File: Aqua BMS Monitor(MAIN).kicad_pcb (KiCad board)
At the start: 4 copper layers, 142 x 101.5 mm, 242 parts, among them J1 UART Jpins, J2 XT60PW-M, J3 XT60PW-M, J4 XT60PW-M, J5 SWD_01x04_Pin, J6 XT60PW-M, J7 USB_C_Female_USB2_Small, Q6 NPN, U1 BQ7695202, U2 STM32F205RETx, U4 LM66100DCKR, U5 LM66100DCKR, U6 LM66100DCKR, U7 LTC4359-DCB, U9 AMS1117-3.3, X1 X322516MRB4SI

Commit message: Not sure
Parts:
- moved U5 30.2 mm to (199.5, 81.7), turned to 0 degrees
- moved C71 30.1 mm to (199.3, 83.8), turned to 0 degrees
- moved U9 18.3 mm to (193.5, 82.2), turned to 0 degrees
- moved TP23 14.0 mm to (222.0, 90.5)
- moved TP5 14.0 mm to (222.0, 95.0)
- moved TP64 14.0 mm to (221.5, 84.0)
- moved TP65 14.0 mm to (221.5, 87.0)
- moved USBC1 9.84 mm to (188.0, 84.7), turned to -90 degrees
- moved USBC2 7.54 mm to (188.0, 80.2), turned to 90 degrees
- moved TP62 7.23 mm to (182.8, 82.7)
- moved USBR3 5.11 mm to (182.8, 90.5)
- moved MCUC14 4.73 mm to (180.8, 89.3), turned to 0 degrees
- moved MCUC21 4.46 mm to (179.2, 87.7)
- moved C72 3.41 mm to (158.1, 87.5)
- moved FB1 3.41 mm to (164.4, 83.0)
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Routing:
- net BAT-: track 221.2 -> 200.9 mm, vias 91 -> 90
- net REG1: track 10.7 -> 23.0 mm, vias 0 -> 2
- net USB_C_VBUS: track 30.0 -> 20.8 mm
- net VDD: track 170.7 -> 176.9 mm
- net ALERT: track 9.13 -> 4.34 mm, vias 1 -> 0
- net Net-(U2-BOOT0): track 47.4 -> 49.0 mm
- net Net-(U2-NRST): track 37.0 -> 36.1 mm

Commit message: Aight
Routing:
- net BAT-: track 200.9 -> 204.9 mm, vias 90 -> 93
- net VDD: track 176.9 -> 178.5 mm
- added copper zone on In2.Cu, net BAT-

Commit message: Final for now
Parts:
- added MCUTVS3: PTVSUC3D5VB, easyeda2kicad:5V_TVS_SOD-323_L1.8-W1.3-LS2.5-BI, F.Cu at (201.8, 100.5)
- added MCUTVS4: PTVSUC3D5VB, easyeda2kicad:5V_TVS_SOD-323_L1.8-W1.3-LS2.5-BI, F.Cu at (204.5, 97.5)
- added TP3: CONN-TP, TestPoint:TestPoint_Pad_1.5x1.5mm, F.Cu at (145.0, 90.5)
- moved TP25 46.6 mm to (164.5, 81.3)
- moved TP24 45.5 mm to (164.4, 86.4)
- moved TP65 43.6 mm to (185.2, 111.1)
- moved TP63 42.8 mm to (154.1, 91.0)
- moved TP70 36.4 mm to (163.9, 100.6)
- moved TP68 35.8 mm to (160.7, 98.8)
- moved TP61 34.4 mm to (177.6, 105.1)
- moved TP64 33.7 mm to (202.5, 111.8)
- moved TP72 32.5 mm to (155.9, 93.5)
- moved TP71 30.0 mm to (158.2, 97.5)
- moved TP5 22.9 mm to (199.7, 99.9)
- moved TP69 22.5 mm to (156.6, 105.1)
- moved TP66 21.5 mm to (156.8, 111.3)
- moved TP23 20.6 mm to (202.2, 96.3)
- moved TP67 14.7 mm to (170.2, 111.3)
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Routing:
- net CFETOFF: track 0.00 -> 51.9 mm, vias 0 -> 2
- net ALERT: track 4.34 -> 51.4 mm, vias 0 -> 4
- net DCHG: track 4.77 -> 48.4 mm, vias 1 -> 3
- net DDSG: track 2.49 -> 40.2 mm, vias 0 -> 3
- net RST_SHUT: track 3.80 -> 37.2 mm, vias 1 -> 3
- net DFETOFF: track 1.71 -> 34.6 mm, vias 1 -> 2
- net MCUCFETOFF: track 0.00 -> 28.4 mm, vias 0 -> 3
- net MCUDFETOFF: track 8.14 -> 22.7 mm, vias 1 -> 2
- net Net-(DD1-K): track 32.5 -> 41.7 mm
- net USART1_RX: track 25.7 -> 34.6 mm
- net VDD: track 178.5 -> 171.7 mm
- net Net-(U2-BOOT0): track 49.0 -> 53.9 mm
- net Net-(U2-VCAP_1): track 1.82 -> 6.32 mm
- net Net-(U2-NRST): track 36.1 -> 39.4 mm
- net SCL: track 24.7 -> 26.7 mm
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- added copper zone on In1.Cu, net BAT-
- removed copper zone on In2.Cu, net BAT-
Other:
- board text added: "U1"

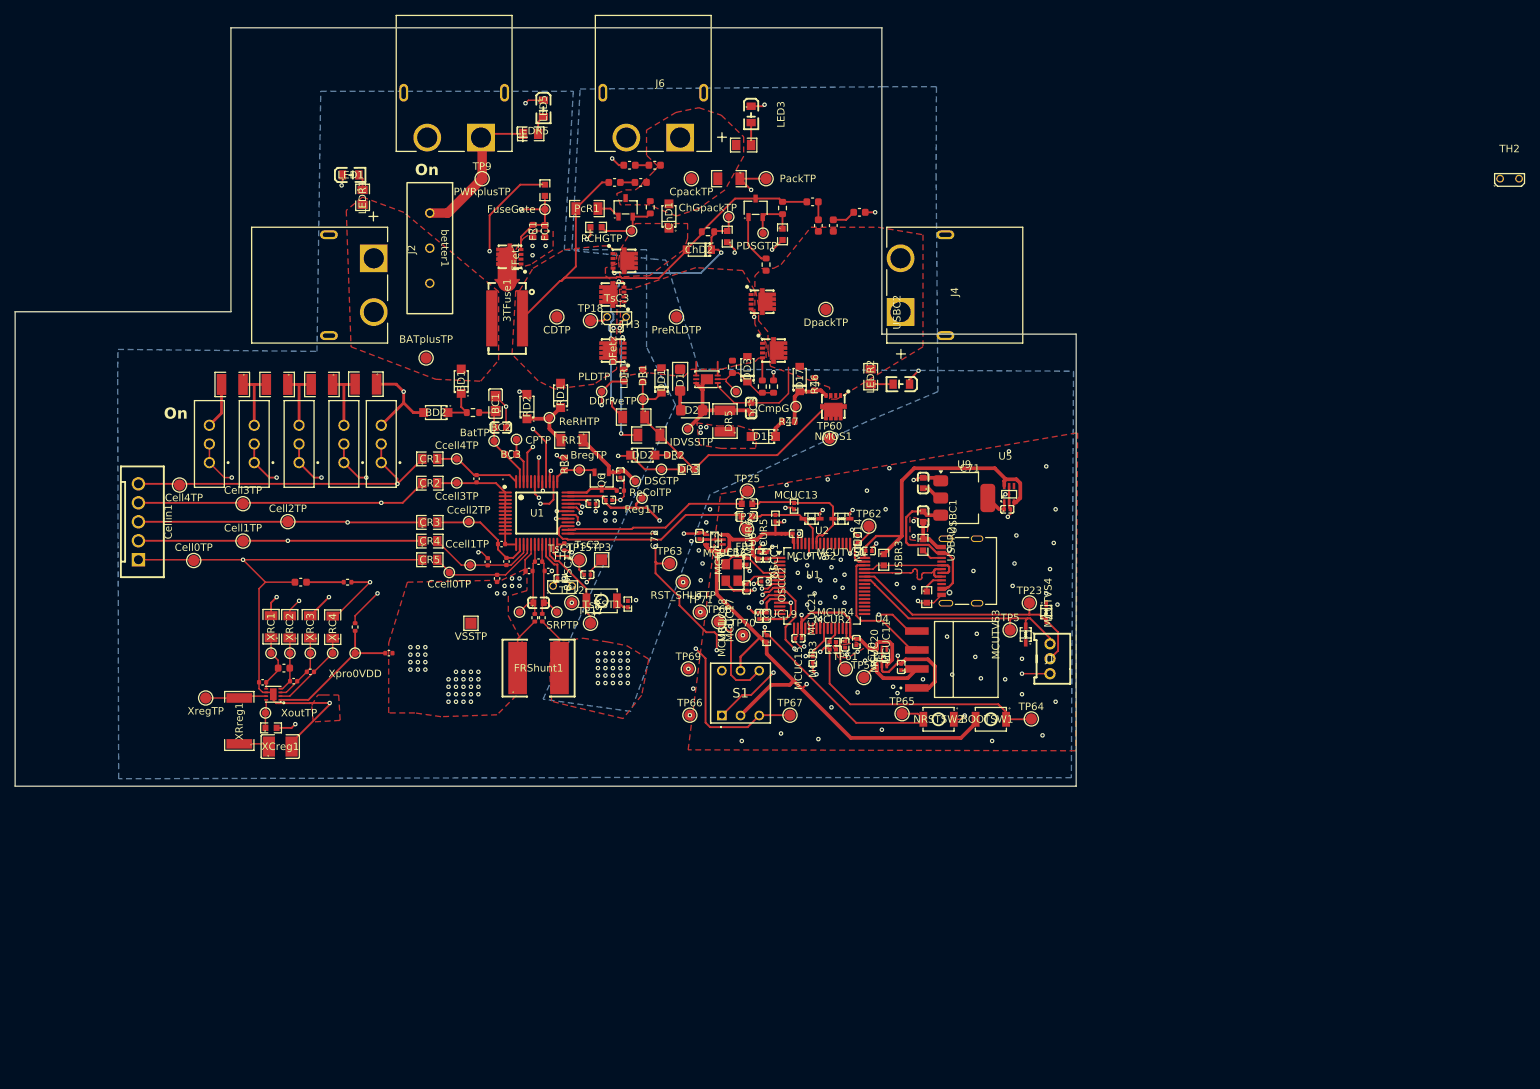
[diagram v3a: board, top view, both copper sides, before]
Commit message: Couple fixes
- Fixed ground plane
- changed thermistor placement
- Attached floating components
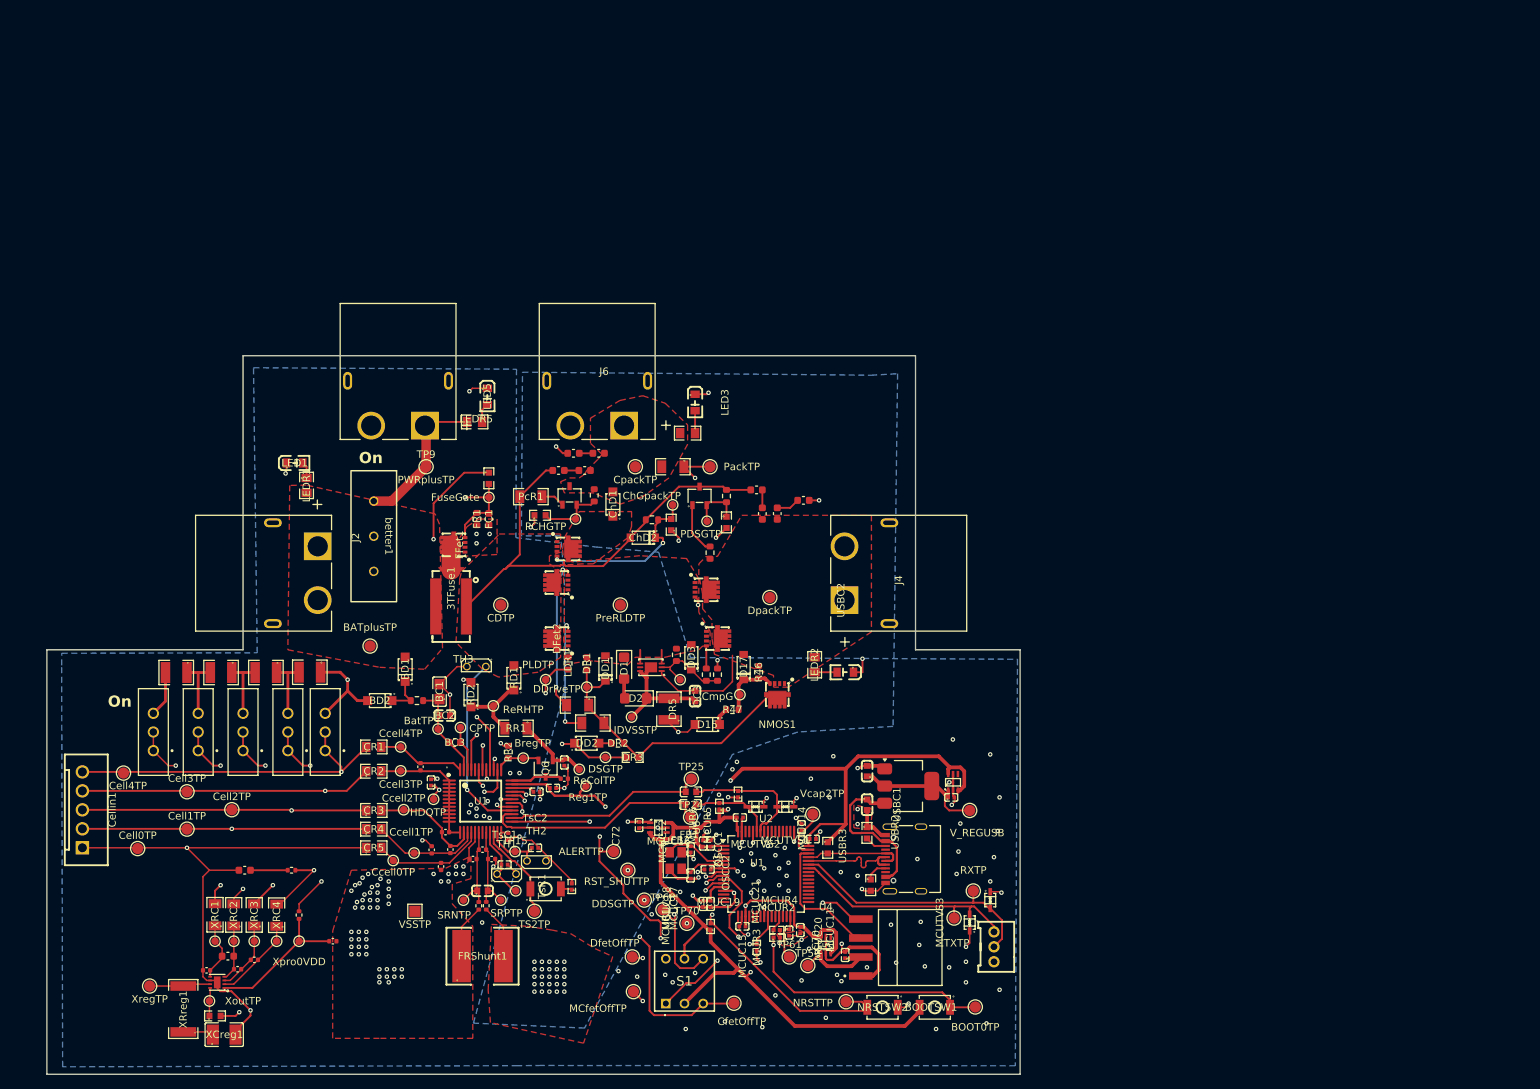
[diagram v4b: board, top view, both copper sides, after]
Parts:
- removed TP3: CONN-TP, TestPoint:TestPoint_Pad_1.5x1.5mm
- TP12, TP15, TP18: footprint TestPoint:TestPoint_Pad_D1.5mm -> TestPoint:TestPoint_Pad_D1.0mm
- moved TH2 159.0 mm to (136.3, 130.8)
- moved TP18 67.4 mm to (122.5, 122.5)
- moved TsC3 65.7 mm to (122.2, 120.3), turned to 90 degrees
- moved TP60 53.2 mm to (194.2, 124.0)
- moved TH3 50.4 mm to (128.2, 104.8), turned to 180 degrees
- moved TP15 40.0 mm to (133.4, 129.6)
- moved C72 39.5 mm to (150.0, 126.0)
- moved TP34 39.5 mm to (118.5, 124.0)
- moved BMSC1 39.5 mm to (132.5, 127.5)
- moved MCUC19 39.3 mm to (159.2, 131.9)
- moved SC2 39.3 mm to (130.3, 130.6)
- moved BC1 39.3 mm to (123.3, 108.2)
- moved BD1 39.3 mm to (118.7, 105.2)
- moved BQ296115DSGR1 39.3 mm to (93.5, 147.1)
- moved C1-0 39.3 mm to (123.5, 131.6)
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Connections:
- U1 pad 44: SCL -> unconnected-(U1-NC-Pad44)
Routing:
- net VDD: track 171.7 -> 191.4 mm, vias 6 -> 7
- net BAT-: track 206.4 -> 222.8 mm, vias 156 -> 170
- net HDQ: track 19.1 -> 31.3 mm, vias 1 -> 2
- net V_REGUSB: track 6.60 -> 18.1 mm
- net Net-(U2-BOOT0): track 53.9 -> 51.3 mm
- net Net-(U2-NRST): track 39.4 -> 41.8 mm
- net SWCLK: track 17.1 -> 18.7 mm
- net Net-(RD1-K): track 8.68 -> 10.2 mm
- net Net-(U1-FUSE): track 55.9 -> 55.2 mm
- net PACK-: track 14.6 -> 15.3 mm
- net MCUCFETOFF: track 28.4 -> 29.1 mm
- net Net-(Dfet1-G): track 21.0 -> 20.4 mm
- net TS3: track 7.25 -> 7.87 mm
- net TS1: track 10.1 -> 9.86 mm, vias 1 -> 0
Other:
- board size 142 x 101.5 mm -> 130.2 x 96.2 mm
- board text added: "Should we have an R here to deter the current path"
- board text removed: "Charge and discharge"
- board text removed: "Clamp"
- board text removed: "MCU"
- board text removed: "Pre-Discharge Charge"
- board text removed: "Shunt resistor setup"
- board text removed: "TPs"
- board text removed: "Thermal measurement"

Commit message: Decorating
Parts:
- added G***: LOGO, easyeda2kicad:Eagle Battery, B.Cu at (138.0, 90.0)
- added G***: LOGO, easyeda2kicad:Aqua Logo, B.Cu at (133.0, 120.8)
- TP37: value Xpro0VDD -> Xpro0VDDTP
- TP51: value PLDTP -> LDTP
- TP53: value CmpG -> CmpGTP
- TP60: value V_REGUSB -> V_REGUSBTP
- TP62: value Vcap2TP -> VCAP2TP
- moved TP66 1.53 mm to (148.8, 149.8)
- renumbered BOOTSW1 to BOOT0, TP70 to DCHGTP, TP68 to MCUDFETOFFTP, NRSTSW2 to RESET, TP25 to SCLTP, TP24 to SDATP, TP12 to TS1TP, TP15 to TS3TP, TP61 to VCAP1TP, TP59 to V_SWDTP
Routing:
- net BAT-: vias 170 -> 171
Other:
- board text added: "Battery Management System (BMS) Board aQuatonomous August 2026 Logan Calder Alisa Ruzhynsky"

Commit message: coupla changes
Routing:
- net BAT-: track 222.8 -> 316.4 mm
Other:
- board text removed: "Should we have an R here to deter the current path"
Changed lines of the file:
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@@
 		(property "Reference" "TP57"
 			(at 0 -1.448 0)
-			(layer "F.SilkS")
+			(layer "F.Fab")
 			(hide yes)
 			(effects
@@
 		)
 		(property "Value" "IDGTP"
-			(at 0 1.55 0)
-			(layer "F.Fab")
-			(hide yes)
+			(at -2.9 0.45 0)
+			(layer "F.SilkS")
 			(effects
 				(font
@@
 		(property "Reference" "TP40"
 			(at 0 -1.448 0)
-			(layer "F.SilkS")
+			(layer "F.Fab")
 			(hide yes)
 			(effects
@@
 		)
 		(property "Value" "Xcel1TP"
-			(at 0 1.55 0)
-			(layer "F.Fab")
-			(hide yes)
+			(at -5.45 -0.15 0)
+			(layer "F.SilkS")
 			(effects
 				(font
@@
 		)
 	)
-	(gr_text "Should we have an R here to deter the current path"
-		(at 75.25 157.55 0)
-		(layer "Cmts.User")
-		(effects
-			(font
-				(size 1.5 1.5)
-				(thickness 0.3)
-				(bold yes)
-			)
-			(justify left bottom)
-		)
-	)
 	(gr_text "U1"
 		(at 174.02 93.41 0)
@@
 	)
 	(segment
-		(start 135.625 128.05)
-		(end 137.875 130.3)
-		(width 0.2)
-		(layer "F.Cu")
-		(net "BAT-")
-	)
-	(segment
 		(start 127.25 130.8)
 		(end 127 131.05)
@@
 	)
 	(segment
+		(start 155.25 113.6)
+		(end 155.3 113.55)
+		(width 0.2)
+		(layer "F.Cu")
+		(net "BAT-")
+	)
+	(segment
 		(start 124.7 111.35)
 		(end 124.7 108.55)
@@
 	)
 	(segment
-		(start 154 111.93)
-		(end 154 112.3)
-		(width 0.2)
-		(layer "F.Cu")
-		(net "BAT-")
-	)
-	(segment
 		(start 93.55 147.05)
 		(end 93.55 147.8165)
@@
 	)
 	(segment
+		(start 93.85 156.2)
+		(end 96 154.05)
+		(width 0.254)
+		(layer "F.Cu")
+		(net "BAT-")
+	)
+	(segment
 		(start 137.875 130.3)
 		(end 141 133.425)
@@
 	)
 	(segment
-		(start 154 112.3)
-		(end 155.25 113.55)
-		(width 0.2)
-		(layer "F.Cu")
-		(net "BAT-")
-	)
-	(segment
 		(start 140.48 119.8)
 		(end 140.48 118.8)
@@
 	(segment
 		(start 156.5 113.55)
-		(end 155.25 113.55)
+		(end 157.5 112.55)
 		(width 0.2)
 		(layer "F.Cu")
@@
 	)
 	(segment
-		(start 132.5 128.03)
-		(end 132.77 128.03)
-		(width 0.2)
-		(layer "F.Cu")
-		(net "BAT-")
-	)
-	(segment
 		(start 89.49925 129.04925)
 		(end 89.5 129.05)
@@
 	)
 	(segment
-		(start 157.68 133.17)
-		(end 156.9 133.17)
-		(width 0.3)
+		(start 132.8 128)
+		(end 132.77 128.03)
+		(width 0.2)
 		(layer "F.Cu")
 		(net "BAT-")
 	)
 	(segment
-		(start 132.77 128.03)
-		(end 133.25 127.55)
-		(width 0.2)
+		(start 157.68 133.17)
+		(end 156.9 133.17)
+		(width 0.3)
 		(layer "F.Cu")
 		(net "BAT-")
@@
 	)
 	(segment
-		(start 133.25 127.55)
-		(end 134 127.55)
-		(width 0.2)
-		(layer "F.Cu")
-		(net "BAT-")
-	)
-	(segment
 		(start 171.2475 140.815342)
 		(end 171.5825 140.480342)
@@
 	)
 	(segment
+		(start 135.625 128.05)
+		(end 137.875 130.3)
+		(width 0.2)
+		(layer "F.Cu")
+		(net "BAT-")
+	)
+	(segment
 		(start 175.005 143.885342)
 		(end 175.005 143.160342)
@@
 	)
 	(segment
+		(start 155.3 113.55)
+		(end 156.5 113.55)
+		(width 0.2)
+		(layer "F.Cu")
+		(net "BAT-")
+	)
+	(segment
 		(start 125.65 104.8)
 		(end 123.3 107.15)
@@
 	)
 	(segment
-		(start 134 127.55)
-		(end 134.5 128.05)
-		(width 0.2)
+		(start 84.2 156.2)
+		(end 93.85 156.2)
+		(width 0.254)
 		(layer "F.Cu")
 		(net "BAT-")
@@
 	)
 	(segment
+		(start 155.25 113.6)
+		(end 155.25 113.55)
+		(width 0.2)
+		(layer "F.Cu")
+		(net "BAT-")
+	)
+	(segment
 		(start 166.7025 123.560342)
 		(end 166.7025 122.775342)
@@
 	)
 	(segment
-		(start 134.5 128.05)
-		(end 135.625 128.05)
-		(width 0.2)
-		(layer "F.Cu")
-		(net "BAT-")
-	)
-	(segment
 		(start 179.25 118.375)
 		(end 179.530892 118.375)
@@
 	)
 	(segment
+		(start 134.5 128.05)
+		(end 135.625 128.05)
+		(width 0.2)
+		(layer "F.Cu")
+		(net "BAT-")
+	)
+	(segment
 		(start 136.75 122.55)
 		(end 136.75 121.6)
@@
 	)
 	(segment
+		(start 133.4 128)
+		(end 134.45 128)
+		(width 0.2)
+		(layer "F.Cu")
+		(net "BAT-")
+	)
+	(segment
 		(start 140 121.05)
 		(end 140.48 120.57)
@@
 	)
 	(segment
+		(start 133.4 128)
+		(end 132.8 128)
+		(width 0.2)
+		(layer "F.Cu")
+		(net "BAT-")
+	)
+	(segment
 		(start 159.5825 136.140342)
 		(end 158.5825 136.140342)
@@
 	)
 	(segment
+		(start 132.77 128.03)
+		(end 132.5 128.03)
+		(width 0.2)
+		(layer "F.Cu")
+		(net "BAT-")
+	)
+	(segment
 		(start 157.2 135.502842)
 		(end 157.8375 136.140342)
@@
 	)
 	(segment
+		(start 155.25 113.55)
+		(end 154 112.3)
+		(width 0.2)
+		(layer "F.Cu")
+		(net "BAT-")
+	)
+	(segment
 		(start 92.6 146.8)
 		(end 92.1335 146.8)
@@
 	)
 	(segment
+		(start 134.45 128)
+		(end 134.5 128.05)
+		(width 0.2)
+		(layer "F.Cu")
+		(net "BAT-")
+	)
+	(segment
 		(start 192.274879 122.303855)
 		(end 192.274879 122.883855)
@@
 	)
 	(segment
-		(start 157.5 112.55)
-		(end 156.5 113.55)
-		(width 0.2)
-		(layer "F.Cu")
-		(net "BAT-")
-	)
-	(segment
 		(start 94.315882 148.2445)
 		(end 94.313882 148.2425)
@@
 	)
 	(segment
+		(start 154 112.3)
+		(end 154 111.93)
+		(width 0.2)
+		(layer "F.Cu")
+		(net "BAT-")
+	)
+	(segment
 		(start 158.5825 128.060342)
 		(end 159.5825 128.060342)
@@
 	)
 	(via
-		(at 98 150.8)
+		(at 179.25 132.8)
 		(size 0.6)
 		(drill 0.3)
 		(layers "F.Cu" "B.Cu")
+		(free yes)
 		(net "BAT-")
 	)
 	(via
-		(at 179.25 132.8)
+		(at 136.75 122.55)
 		(size 0.6)
 		(drill 0.3)
 		(layers "F.Cu" "B.Cu")
-		(free yes)
 		(net "BAT-")
 	)
 	(via
-		(at 136.75 122.55)
+		(at 84.2 156.2)
 		(size 0.6)
 		(drill 0.3)
@@
 	)
 	(via
-		(at 134 127.55)
+		(at 133.4 128)
 		(size 0.6)
 		(drill 0.3)
@@
 	)
 	(via
-		(at 155.25 113.55)
+		(at 155.25 113.6)
 		(size 0.6)
 		(drill 0.3)
@@
 	)
 	(segment
+		(start 99.4 103.4)
+		(end 81 103.4)
+		(width 0.254)
+		(layer "B.Cu")
+		(net "BAT-")
+	)
+	(segment
+		(start 81.8 156.2)
+		(end 84.2 156.2)
+		(width 0.254)
+		(layer "B.Cu")
+		(net "BAT-")
+	)
+	(segment
+		(start 72.2 112.2)
+		(end 72.2 146.6)
+		(width 0.254)
+		(layer "B.Cu")
+		(net "BAT-")
+	)
+	(segment
+		(start 72.2 146.6)
+		(end 81.8 156.2)
+		(width 0.254)
+		(layer "B.Cu")
+		(net "BAT-")
+	)
+	(segment
+		(start 81 103.4)
+		(end 72.2 112.2)
+		(width 0.254)
+		(layer "B.Cu")
+		(net "BAT-")
+	)
+	(segment
 		(start 89.5 129.05)
 		(end 89.5 119.55)
@@
 				(xy 98.379281 65.101571) (xy 133.6 65) (xy 133.52154 87.55) (xy 144.3 88.802535) (xy 152.62058 89.484199)
 				(xy 156.8698 103.583883) (xy 200.568737 103.656143) (xy 200.478252 158.376463) (xy 136.929169 158.182404)
-				(xy 133.747163 158.186894) (xy 72.856111 158.356475) (xy 72.723327 104.621794) (xy 72.720706 102.992097)
-				(xy 98.488379 102.932376)
+				(xy 86.80082 158.212785) (xy 86.799166 134) (xy 86.739272 134) (xy 86.860109 102.959325) (xy 98.488379 102.932376)
 			)
 		)
